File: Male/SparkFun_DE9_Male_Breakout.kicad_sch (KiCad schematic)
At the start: 9 parts, among them J1 Conn_01x01, J2 Conn_01x09, J3 DE9-Male, J4 Conn_01x01

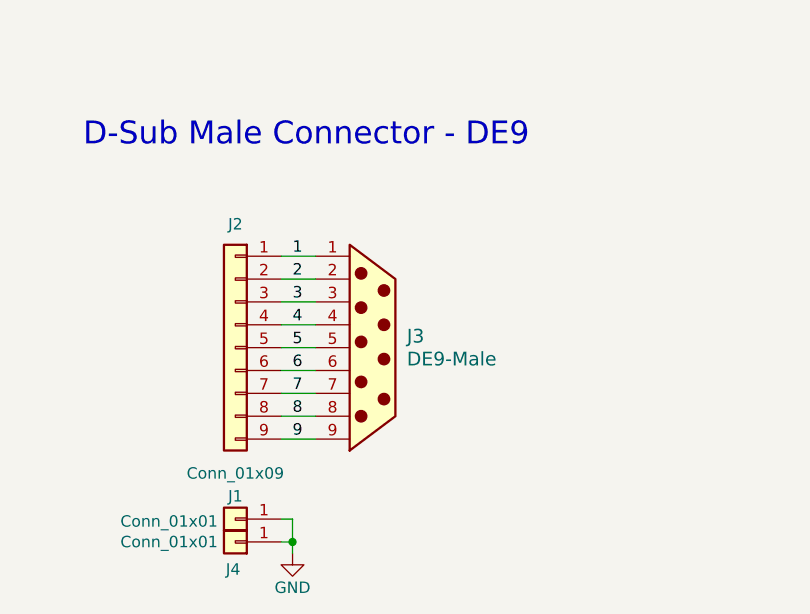
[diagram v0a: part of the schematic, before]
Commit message: Updates DE9 layout by placing components more consistently on grid
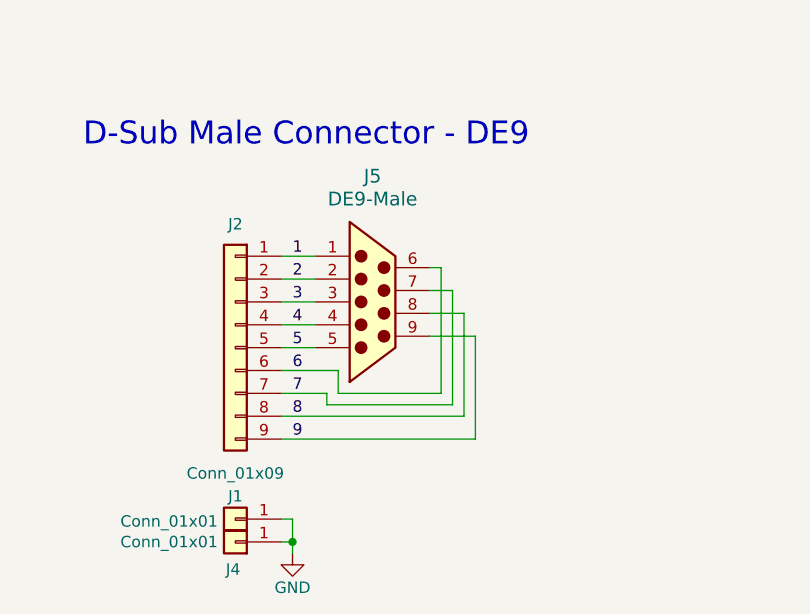
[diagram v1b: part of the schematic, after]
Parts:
- removed J3: DE9-Male, DE9-Footprint:DB9, symbol DB9-Male:DE9-Male
- added J5: DE9-Male, DE9-Footprint:DE9, symbol DE9-Male:DE9-Male
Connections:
- net 1: now also J5.1
- net 2: now also J5.2
- net 3: now also J5.3
- net 4: now also J5.4
- net 5: now also J5.5
- net 6: now also J5.6
- net 7: now also J5.7
- net 8: now also J5.8
- net 9: now also J5.9
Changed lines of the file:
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@@
-	(wire
-		(pts
-			(xy 67.31 105.41) (xy 71.12 105.41)
-		)
-		(stroke
-			(width 0.2286)
-			(type default)
-		)
-	)
 	(wire
 		(pts
@@
 	(wire
 		(pts
-			(xy 67.31 100.33) (xy 71.12 100.33)
+			(xy 72.39 101.6) (xy 72.39 100.33)
+		)
+		(stroke
+			(width 0)
+			(type default)
+		)
+	)
+	(wire
+		(pts
+			(xy 67.31 100.33) (xy 72.39 100.33)
+		)
+		(stroke
+			(width 0)
+			(type default)
+		)
+	)
+	(wire
+		(pts
+			(xy 86.36 88.9) (xy 86.36 101.6)
 		)
 		(stroke
@@
 	(wire
 		(pts
+			(xy 67.31 105.41) (xy 88.9 105.41)
+		)
+		(stroke
+			(width 0)
+			(type default)
+		)
+	)
+	(wire
+		(pts
+			(xy 88.9 93.98) (xy 88.9 105.41)
+		)
+		(stroke
+			(width 0)
+			(type default)
+		)
+	)
+	(wire
+		(pts
 			(xy 67.31 90.17) (xy 71.12 90.17)
 		)
@@
 	(wire
 		(pts
+			(xy 85.09 86.36) (xy 83.82 86.36)
+		)
+		(stroke
+			(width 0)
+			(type default)
+		)
+	)
+	(wire
+		(pts
 			(xy 67.31 92.71) (xy 71.12 92.71)
 		)
@@
 		)
 	)
+	(wire
+		(pts
+			(xy 87.63 102.87) (xy 87.63 91.44)
+		)
+		(stroke
+			(width 0)
+			(type default)
+		)
+	)
+	(wire
+		(pts
+			(xy 83.82 93.98) (xy 88.9 93.98)
+		)
+		(stroke
+			(width 0)
+			(type default)
+		)
+	)
+	(wire
+		(pts
+			(xy 86.36 101.6) (xy 72.39 101.6)
+		)
+		(stroke
+			(width 0)
+			(type default)
+		)
+	)
 	(polyline
 		(pts
@@
 	(wire
 		(pts
+			(xy 73.66 100.33) (xy 85.09 100.33)
+		)
+		(stroke
+			(width 0)
+			(type default)
+		)
+	)
+	(wire
+		(pts
 			(xy 68.58 114.3) (xy 68.58 116.84)
 		)
@@
 	(wire
 		(pts
-			(xy 67.31 97.79) (xy 71.12 97.79)
+			(xy 73.66 97.79) (xy 73.66 100.33)
+		)
+		(stroke
+			(width 0)
+			(type default)
+		)
+	)
+	(wire
+		(pts
+			(xy 67.31 97.79) (xy 73.66 97.79)
 		)
 		(stroke
@@
 	(wire
 		(pts
-			(xy 67.31 102.87) (xy 71.12 102.87)
+			(xy 83.82 88.9) (xy 86.36 88.9)
+		)
+		(stroke
+			(width 0)
+			(type default)
+		)
+	)
+	(wire
+		(pts
+			(xy 85.09 100.33) (xy 85.09 86.36)
+		)
+		(stroke
+			(width 0)
+			(type default)
+		)
+	)
+	(wire
+		(pts
+			(xy 67.31 102.87) (xy 87.63 102.87)
 		)
 		(stroke
@@
 		(pts
 			(xy 67.31 114.3) (xy 68.58 114.3)
+		)
+		(stroke
+			(width 0)
+			(type default)
+		)
+	)
+	(wire
+		(pts
+			(xy 87.63 91.44) (xy 83.82 91.44)
 		)
 		(stroke
@@
 				(path "/e3dd3ae4-244d-4cba-9cca-5d2abf83f29a"
 					(reference "ST2")
+					(unit 1)
+				)
+			)
+		)
+	)
+	(symbol
+		(lib_name "DE9-Male_1")
+		(lib_id "DE9-Male:DE9-Male")
+		(at 77.47 92.71 0)
+		(unit 1)
+		(exclude_from_sim no)
+		(in_bom yes)
+		(on_board yes)
+		(dnp no)
+		(fields_autoplaced yes)
+		(property "Reference" "J5"
+			(at 77.47 76.2 0)
+			(effects
+				(font
+					(size 1.524 1.524)
+				)
+			)
+		)
+		(property "Value" "DE9-Male"
+			(at 77.47 78.74 0)
+			(effects
+				(font
+					(size 1.524 1.524)
+				)
+			)
+		)
+		(property "Footprint" "DE9-Footprint:DE9"
+			(at 77.47 104.394 0)
+			(effects
+				(font
+					(size 1.27 1.27)
+					(italic yes)
+				)
+				(hide yes)
+			)
+		)
+		(property "Datasheet" ""
+			(at 75.692 112.014 0)
+			(effects
+				(font
+					(size 1.27 1.27)
+					(italic yes)
+				)
+				(hide yes)
+			)
+		)
+		(property "Description" ""
+			(at 77.47 92.71 0)
+			(effects
+				(font
+					(size 1.27 1.27)
+				)
+				(hide yes)
+			)
+		)
+		(pin "8"
+		)
+		(pin "7"
+		)
+		(pin "5"
+		)
+		(pin "6"
+		)
+		(pin "3"
+		)
+		(pin "4"
+		)
+		(pin "2"
+		)
+		(pin "1"
+		)
+		(pin "9"
+		)
+		(instances
+			(project ""
+				(path "/e3dd3ae4-244d-4cba-9cca-5d2abf83f29a"
+					(reference "J5")
 					(unit 1)
 				)
@@
 					(unit 1)
 				)
-			)
-		)
-	)
-	(symbol
-		(lib_id "DB9-Male:DE9-Male")
-		(at 77.47 95.25 0)
-		(unit 1)
-		(exclude_from_sim no)
-		(in_bom yes)
-		(on_board yes)
-		(dnp no)
-		(fields_autoplaced yes)
-		(property "Reference" "J3"
-			(at 81.28 93.9799 0)
-			(effects
-				(font
-					(size 1.524 1.524)
-				)
-				(justify left)
-			)
-		)
-		(property "Value" "DE9-Male"
-			(at 81.28 96.5199 0)
-			(effects
-				(font
-					(size 1.524 1.524)
-				)
-				(justify left)
-			)
-		)
-		(property "Footprint" "DE9-Footprint:DB9"
-			(at 76.454 112.268 0)
-			(effects
-				(font
-					(size 1.27 1.27)
-					(italic yes)
-				)
-				(hide yes)
-			)
-		)
-		(property "Datasheet" ""
-			(at 75.692 114.554 0)
-			(effects
-				(font
-					(size 1.27 1.27)
-					(italic yes)
-				)
-				(hide yes)
-			)
-		)
-		(property "Description" ""
-			(at 77.47 95.25 0)
-			(effects
-				(font
-					(size 1.27 1.27)
-				)
-				(hide yes)
-			)
-		)
-		(pin "8"
-		)
-		(pin "5"
-		)
-		(pin "4"
-		)
-		(pin "3"
-		)
-		(pin "2"
-		)
-		(pin "1"
-		)
-		(pin "9"
-		)
-		(pin "7"
-		)
-		(pin "6"
-		)
-		(instances
-			(project ""
-				(path "/e3dd3ae4-244d-4cba-9cca-5d2abf83f29a"
-					(reference "J3")
-					(unit 1)
-				)

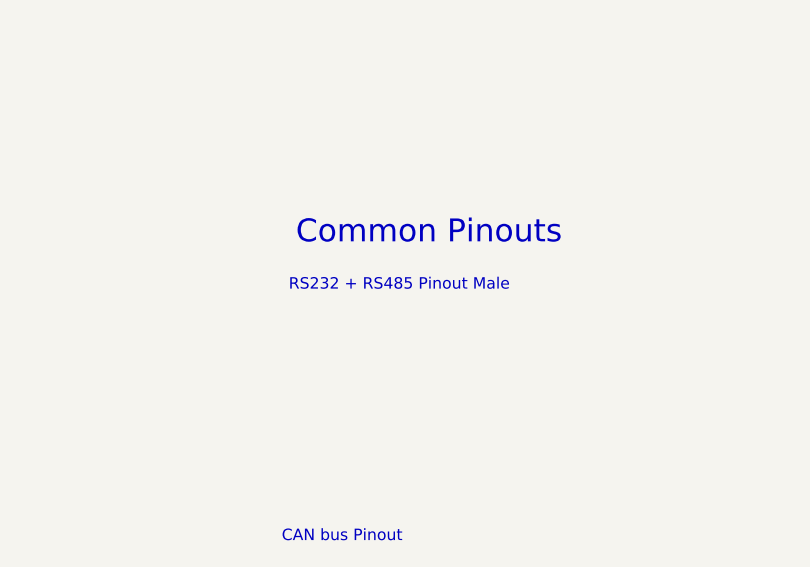
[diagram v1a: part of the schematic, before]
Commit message: Fixes common pinouts tables in schematics
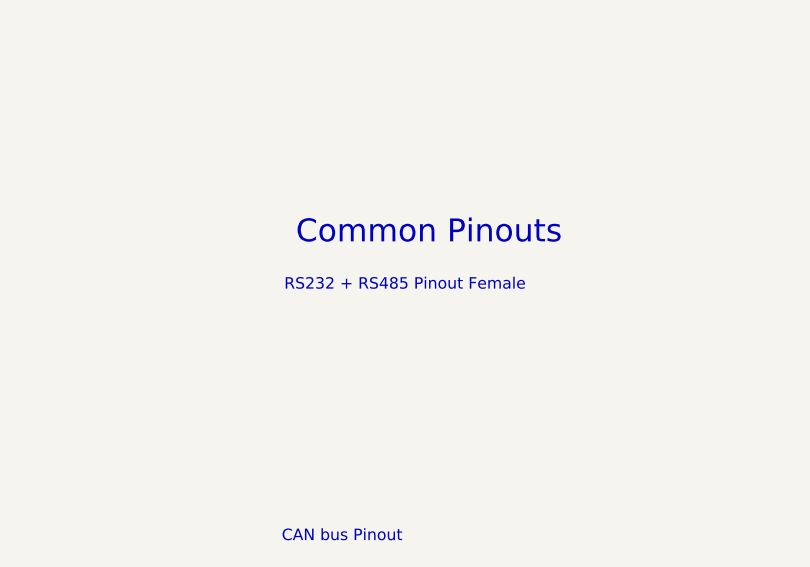
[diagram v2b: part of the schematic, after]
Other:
- note added: "RS232 + RS485 Pinout Female"
- note removed: "RS232 + RS485 Pinout Male"
